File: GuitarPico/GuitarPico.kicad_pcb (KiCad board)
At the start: 2 copper layers, 100 x 100 mm, 125 parts, among them J1 INPUT, J2 INPUT, J3 OUTPUT, J4 OUTPUT, J5 Barrel_Jack_Switch, J6 VGA, J8 INPUT, J9 INPUT, Q1 2N3904, Q2 2N3904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

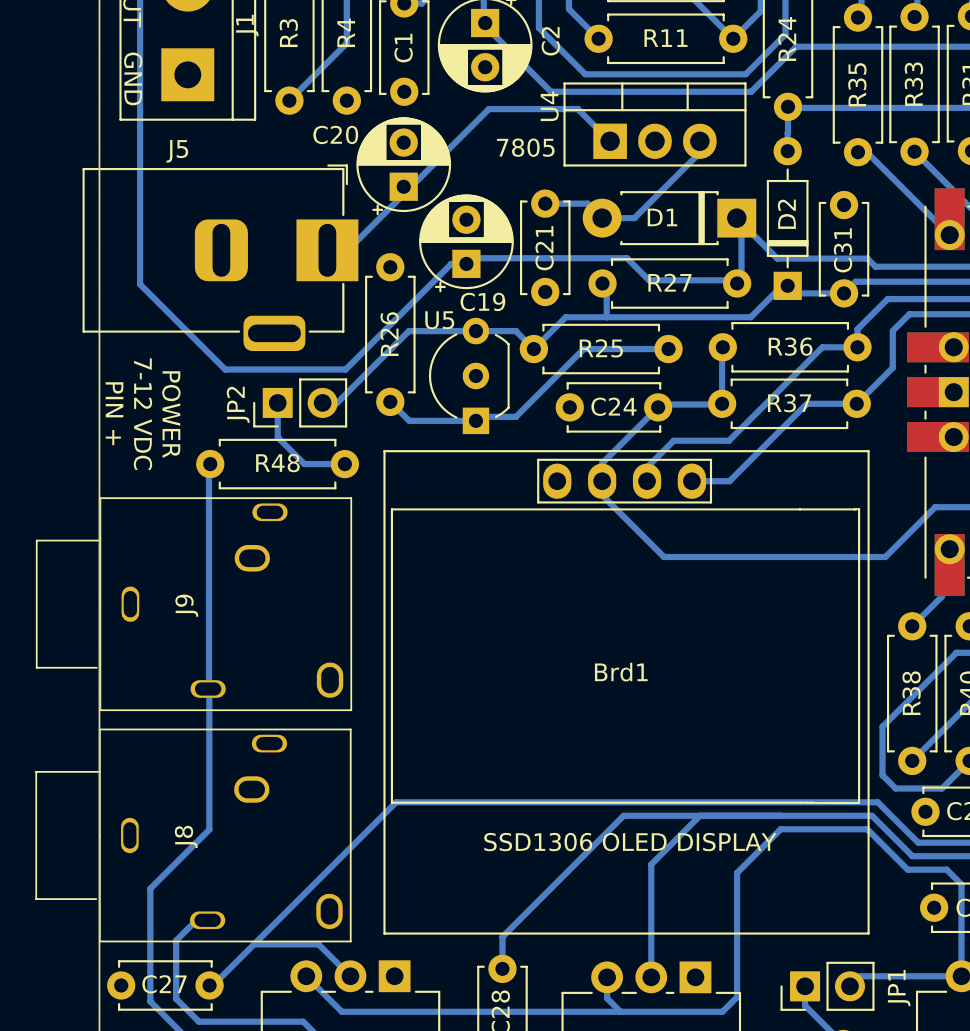
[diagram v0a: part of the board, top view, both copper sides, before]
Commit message: Added FIR Filter examples
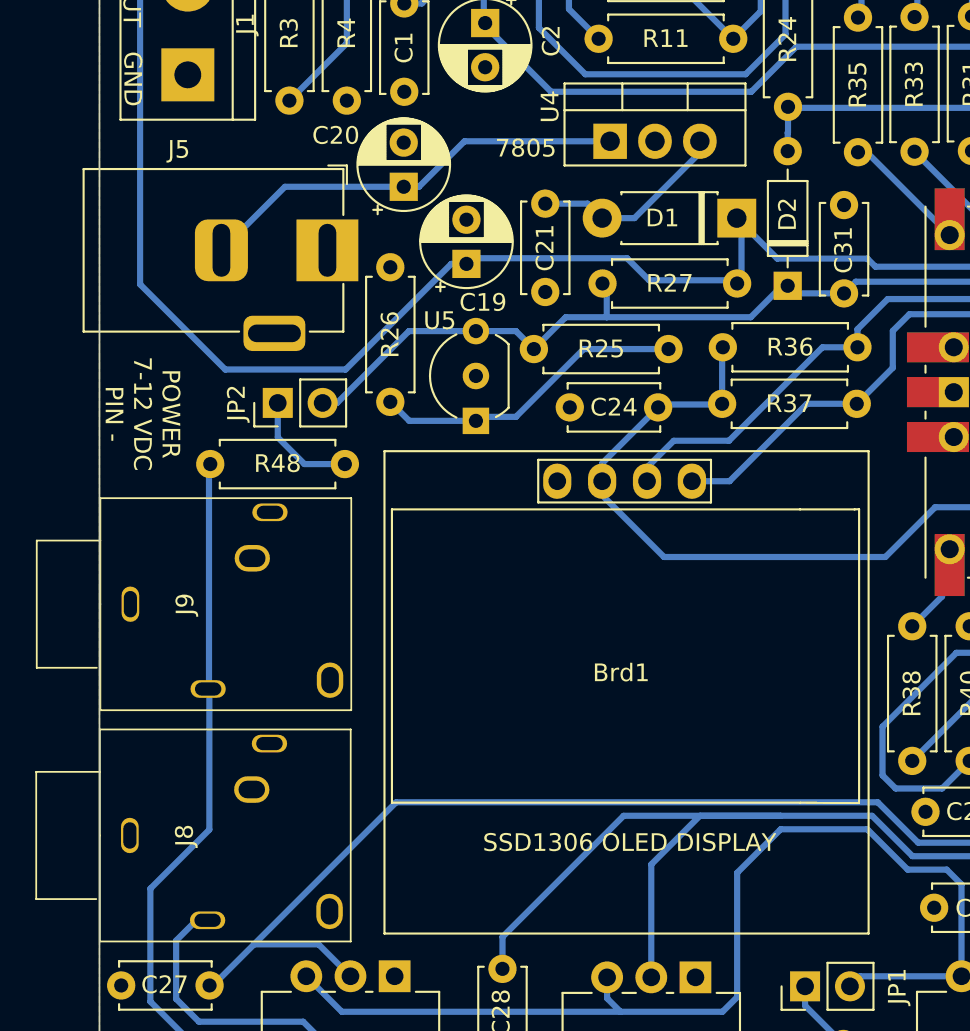
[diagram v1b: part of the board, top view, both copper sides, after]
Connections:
- J5 pad 1: Net-(C20-Pad1) -> GND
- J5 pad 2: GND -> Net-(C20-Pad1)
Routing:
- net Net-(C20-Pad1): track 20.1 -> 24.6 mm
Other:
- board text added: "POWER 7-12 VDC PIN -"
- board text removed: "POWER 7-12 VDC PIN +"
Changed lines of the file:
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@@
     (fp_line (start -0.003213 -4.505425) (end 0.8 -3.75) (layer "F.Fab") (width 0.1))
     (pad "1" thru_hole rect (at 0 0) (size 3.5 3.5) (drill oval 1 3) (layers *.Cu *.Mask)
-      (net 38 "Net-(C20-Pad1)") (pintype "passive"))
-    (pad "2" thru_hole roundrect (at -6 0) (size 3 3.5) (drill oval 1 3) (layers *.Cu *.Mask) (roundrect_rratio 0.25)
       (net 2 "GND") (pintype "passive"))
+    (pad "2" thru_hole roundrect (at -6 0) (size 3 3.5) (drill oval 1 3) (layers *.Cu *.Mask) (roundrect_rratio 0.25)
+      (net 38 "Net-(C20-Pad1)") (pintype "passive"))
     (pad "3" thru_hole roundrect (at -3 4.7) (size 3.5 2) (drill oval 3 1) (layers *.Cu *.Mask) (roundrect_rratio 0.25)
       (net 37 "unconnected-(J5-Pad3)") (pintype "passive"))
@@
       (effects (font (size 1 1) (thickness 0.15)))
     )
-    (fp_line (start 5.08 -11.811) (end 5.08 -9.398) (layer "F.SilkS") (width 0.12))
-    (fp_line (start -13.4 15) (end -13.4 -12.3) (layer "F.SilkS") (width 0.12))
+    (fp_line (start 10.122 7.595) (end 13.462 7.62) (layer "F.SilkS") (width 0.12))
+    (fp_line (start 13.462 7.62) (end 13.462 -9.017) (layer "F.SilkS") (width 0.12))
+    (fp_line (start 14 15) (end -13.4 15) (layer "F.SilkS") (width 0.12))
+    (fp_line (start 14 -12.3) (end 14 15) (layer "F.SilkS") (width 0.12))
+    (fp_line (start -12.978 -9.005) (end 10.122 -9.005) (layer "F.SilkS") (width 0.12))
     (fp_line (start 10.122 -9.005) (end 13.208 -9.005) (layer "F.SilkS") (width 0.12))
+    (fp_line (start -12.978 7.595) (end -12.978 -9.005) (layer "F.SilkS") (width 0.12))
+    (fp_line (start 10.122 7.595) (end -12.978 7.595) (layer "F.SilkS") (width 0.12))
     (fp_line (start 13.462 -9.017) (end 13.208 -9.005) (layer "F.SilkS") (width 0.12))
-    (fp_line (start 13.462 7.62) (end 13.462 -9.017) (layer "F.SilkS") (width 0.12))
+    (fp_line (start 5.08 -11.811) (end 5.08 -9.398) (layer "F.SilkS") (width 0.12))
     (fp_line (start 5.08 -9.398) (end -4.699 -9.398) (layer "F.SilkS") (width 0.12))
-    (fp_line (start 10.122 7.595) (end 13.462 7.62) (layer "F.SilkS") (width 0.12))
-    (fp_line (start 10.122 7.595) (end -12.978 7.595) (layer "F.SilkS") (width 0.12))
     (fp_line (start -4.699 -11.811) (end -4.699 -9.398) (layer "F.SilkS") (width 0.12))
-    (fp_line (start 14 -12.3) (end 14 15) (layer "F.SilkS") (width 0.12))
-    (fp_line (start -13.4 -12.3) (end 14 -12.3) (layer "F.SilkS") (width 0.12))
-    (fp_line (start 14 15) (end -13.4 15) (layer "F.SilkS") (width 0.12))
+    (fp_line (start -13.4 15) (end -13.4 -12.3) (layer "F.SilkS") (width 0.12))
     (fp_line (start -4.699 -11.811) (end 5.08 -11.811) (layer "F.SilkS") (width 0.12))
-    (fp_line (start -12.978 -9.005) (end 10.122 -9.005) (layer "F.SilkS") (width 0.12))
-    (fp_line (start -12.978 7.595) (end -12.978 -9.005) (layer "F.SilkS") (width 0.12))
-    (pad "" np_thru_hole oval (at -11 13) (size 3.6 3.1) (drill oval 3.5 3) (layers F&B.Cu *.Mask))
-    (pad "" np_thru_hole oval (at 12 -10.5) (size 3.6 3.1) (drill oval 3.5 3) (layers F&B.Cu *.Mask))
-    (pad "" np_thru_hole oval (at 12 13) (size 3.6 3.1) (drill oval 3.5 3) (layers F&B.Cu *.Mask))
-    (pad "" np_thru_hole oval (at -11 -10.5) (size 3.6 3.1) (drill oval 3.5 3) (layers F&B.Cu *.Mask))
+    (fp_line (start -13.4 -12.3) (end 14 -12.3) (layer "F.SilkS") (width 0.12))
+    (pad "" np_thru_hole oval (at -10.5 13) (size 5 3.1) (drill oval 4.8 3) (layers F&B.Cu *.Mask))
+    (pad "" np_thru_hole oval (at 11 -10.5) (size 5 3.1) (drill oval 4.8 3) (layers F&B.Cu *.Mask))
+    (pad "" np_thru_hole oval (at -10.5 -10.5) (size 5 3.1) (drill oval 4.8 3) (layers F&B.Cu *.Mask))
+    (pad "" np_thru_hole oval (at 11 13) (size 5 3.1) (drill oval 4.8 3) (layers F&B.Cu *.Mask))
     (pad "1" thru_hole oval (at -3.62 -10.6 90) (size 2 1.6) (drill 1) (layers *.Cu *.Mask)
       (net 2 "GND") (pinfunction "GND") (pintype "input"))
@@
     (effects (font (size 1 1) (thickness 0.15)))
   )
-  (gr_text "POWER\n7-12 VDC\nPIN +" (at 46.425 114.725 270) (layer "F.SilkS")
+  (gr_text "POWER\n7-12 VDC\nPIN -" (at 46.425 114.725 270) (layer "F.SilkS")
     (effects (font (size 1 1) (thickness 0.15)))
   )
@@
   (segment (start 69.23 102.83) (end 71.63 102.83) (width 0.35) (layer "B.Cu") (net 36))
   (segment (start 72.45 103.65) (end 74.28 103.65) (width 0.35) (layer "B.Cu") (net 36))
-  (segment (start 72.9 99.3) (end 71.08 97.48) (width 0.35) (layer "B.Cu") (net 38))
-  (segment (start 66.04 97.48) (end 58.048 105.472) (width 0.35) (layer "B.Cu") (net 38))
-  (segment (start 58.048 105.472) (end 56.902 105.472) (width 0.35) (layer "B.Cu") (net 38))
-  (segment (start 71.08 97.48) (end 66.04 97.48) (width 0.35) (layer "B.Cu") (net 38))
+  (segment (start 61.22 101.876) (end 62.084 101.876) (width 0.35) (layer "B.Cu") (net 38))
+  (segment (start 61.22 101.876) (end 54.498 101.876) (width 0.35) (layer "B.Cu") (net 38))
+  (segment (start 54.498 101.876) (end 50.902 105.472) (width 0.35) (layer "B.Cu") (net 38))
+  (segment (start 62.084 101.876) (end 64.66 99.3) (width 0.35) (layer "B.Cu") (net 38))
+  (segment (start 64.66 99.3) (end 72.9 99.3) (width 0.35) (layer "B.Cu") (net 38))
   (segment (start 70.57 88.34) (end 70.57 91.82) (width 0.35) (layer "B.Cu") (net 39))
   (segment (start 73 81.75) (end 73.75 82.5) (width 0.35) (layer "B.Cu") (net 39))

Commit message: First example of guitarpico project
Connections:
- R12 pad 2: Net-(R12-Pad2) -> Net-(C9-Pad1)
- R24 pad 2: Net-(R12-Pad2) -> Net-(C9-Pad1)
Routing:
- net Net-(C9-Pad1): track 17.8 -> 43.4 mm
- net Net-(R12-Pad2): track 23.8 -> 0.00 mm

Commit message: Working pass thru
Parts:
- added C32: 220 uF, Capacitor_THT:CP_Radial_D5.0mm_P2.50mm, F.Cu at (79.6, 123.2)
- added C33: 220 uF, Capacitor_THT:CP_Radial_D5.0mm_P2.50mm, F.Cu at (79.5, 131.0)
- added R58: 10R, Resistor_THT:R_Axial_DIN0207_L6.3mm_D2.5mm_P7.62mm_Horizontal, F.Cu at (85.0, 123.5)
- C9: value 47 pF -> 220 pF
- R24: value 10k -> 100
- R9: value 10k -> 47k
- moved R36 1.18 mm to (80.0, 111.9)
- moved R37 1.16 mm to (87.6, 115.0)
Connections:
- Brd1 pad 2: +3V3 -> Net-(Brd1-Pad2)
- C24 pad 2: +3V3 -> Net-(Brd1-Pad2)
- RV1 pad 1: Net-(C7-Pad2) -> Net-(R5-Pad1)
- RV1 pad 3: Net-(R5-Pad1) -> Net-(C7-Pad2)
- RV2 pad 1: Net-(C17-Pad1) -> Net-(R17-Pad1)
- RV2 pad 3: Net-(R17-Pad1) -> Net-(C17-Pad1)
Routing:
- net Net-(Brd1-Pad2): track 0.00 -> 35.5 mm
- net Net-(R17-Pad1): track 47.6 -> 61.3 mm
- net +3V3: track 135.5 -> 122.7 mm
- net Net-(C17-Pad1): track 61.2 -> 51.2 mm
- net SDA: track 38.1 -> 46.8 mm
- net SCL: track 38.2 -> 42.6 mm
- net Net-(C7-Pad2): track 35.8 -> 39.1 mm
- net Net-(R5-Pad1): track 36.6 -> 34.7 mm
- net VREF: track 231.1 -> 230.4 mm

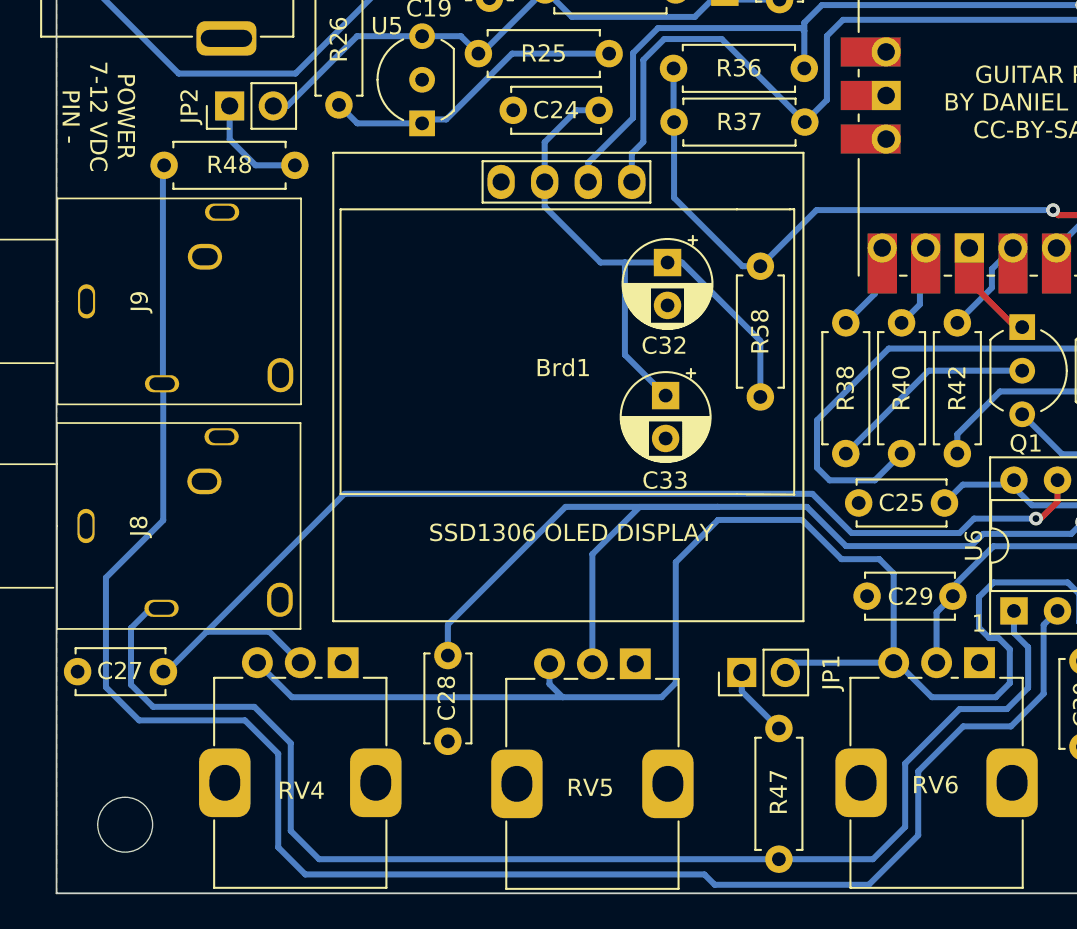
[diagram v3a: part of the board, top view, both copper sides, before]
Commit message: Added ui elements
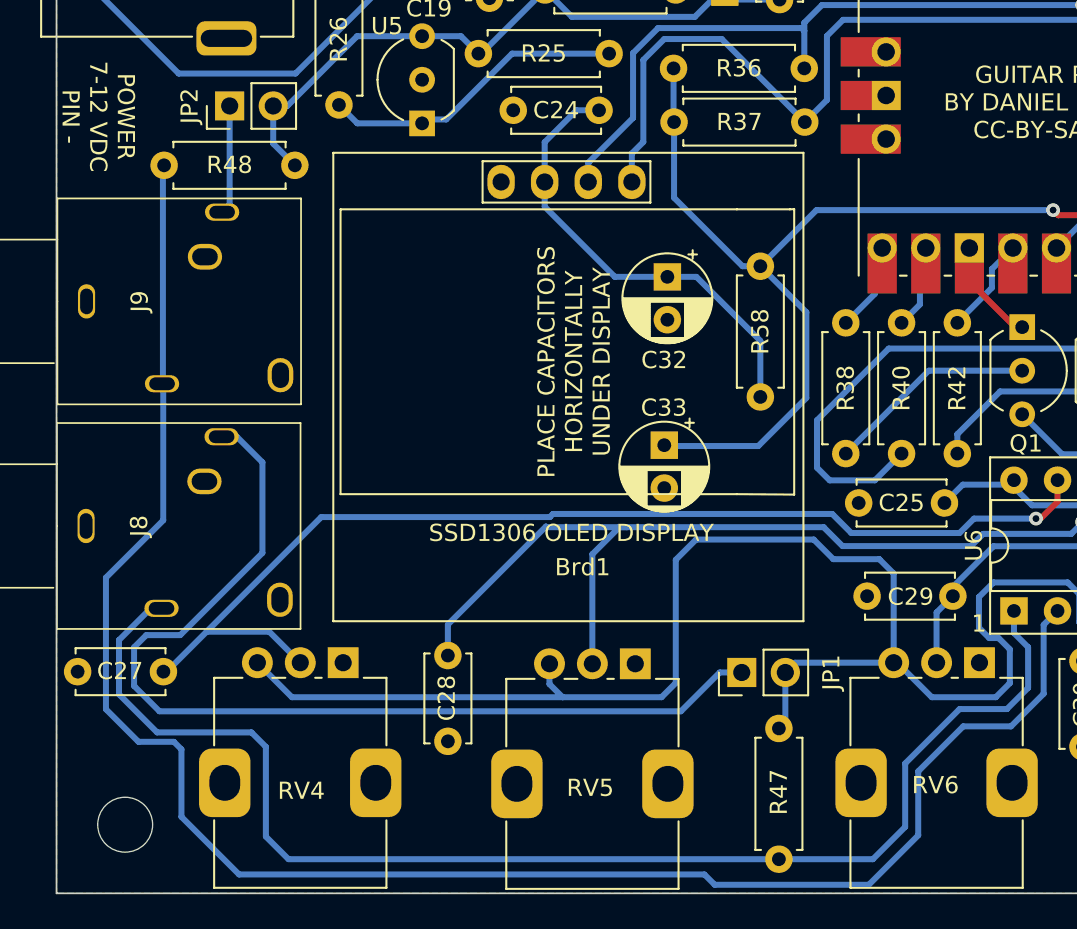
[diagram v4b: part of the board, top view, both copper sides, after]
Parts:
- R47, R48: value 10k -> NC
- moved C33 2.89 mm to (79.4, 133.9)
- moved C32 0.84 mm to (79.6, 124.1)
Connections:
- C33 pad 1: Net-(Brd1-Pad2) -> +3V3
- J8 pad S1: unconnected-(J8-PadS1) -> Net-(J8-PadS1)
- J9 pad S1: unconnected-(J9-PadS1) -> Net-(JP2-Pad1)
- JP1 pad 1: Net-(JP1-Pad1) -> Net-(J8-PadS1)
- R47 pad 1: Net-(JP1-Pad1) -> VREF
- R48 pad 1: Net-(JP2-Pad1) -> VREF
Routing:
- net Net-(J8-PadS1): track 0.00 -> 57.3 mm
- net +3V3: track 122.7 -> 141.0 mm
- net Net-(Brd1-Pad2): track 35.5 -> 26.8 mm
- net Net-(C28-Pad2): track 60.9 -> 54.2 mm
- net VREF: track 230.4 -> 236.9 mm
- net Net-(JP1-Pad1): track 4.16 -> 0.00 mm
- net Net-(J8-PadT1): track 76.2 -> 77.6 mm
- net Net-(C27-Pad2): track 65.6 -> 64.6 mm
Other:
- board text added: "PLACE CAPACITORS HORIZONTALLY UNDER DISPLAY"

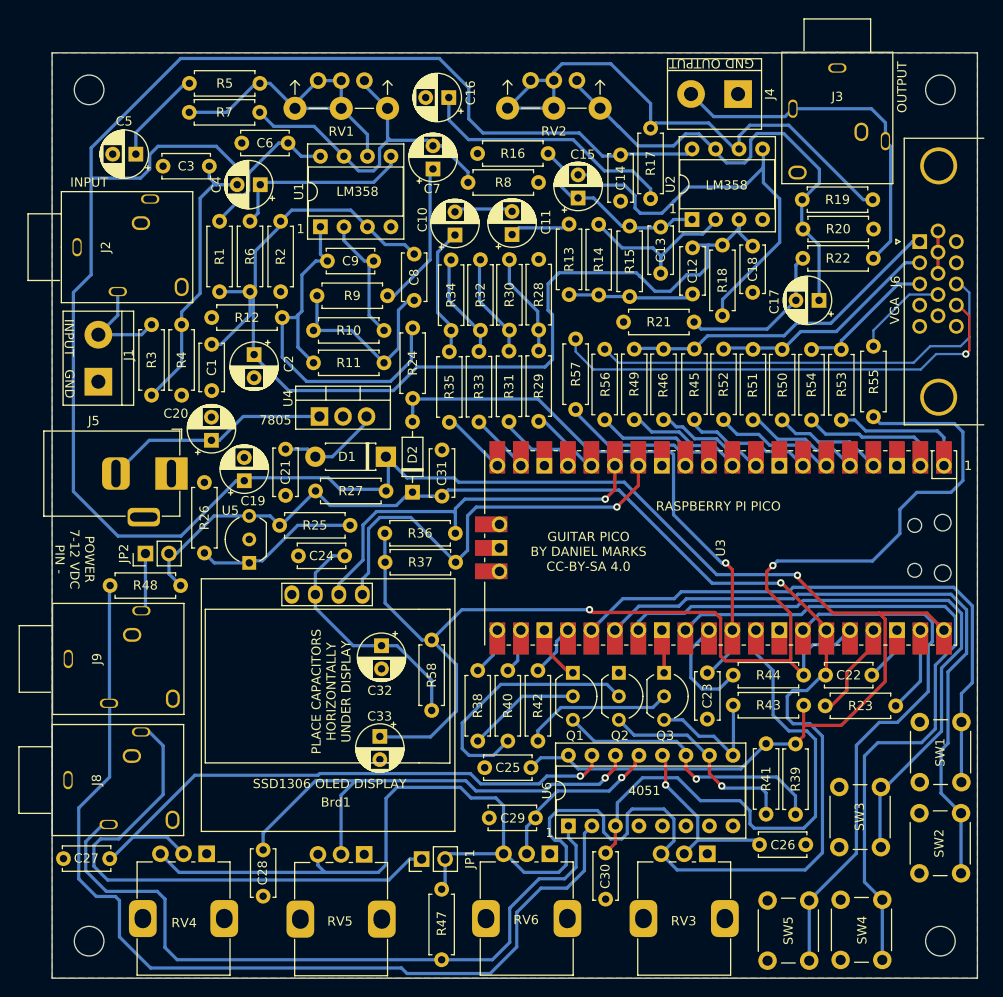
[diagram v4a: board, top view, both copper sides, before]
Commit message: can now edit parameters
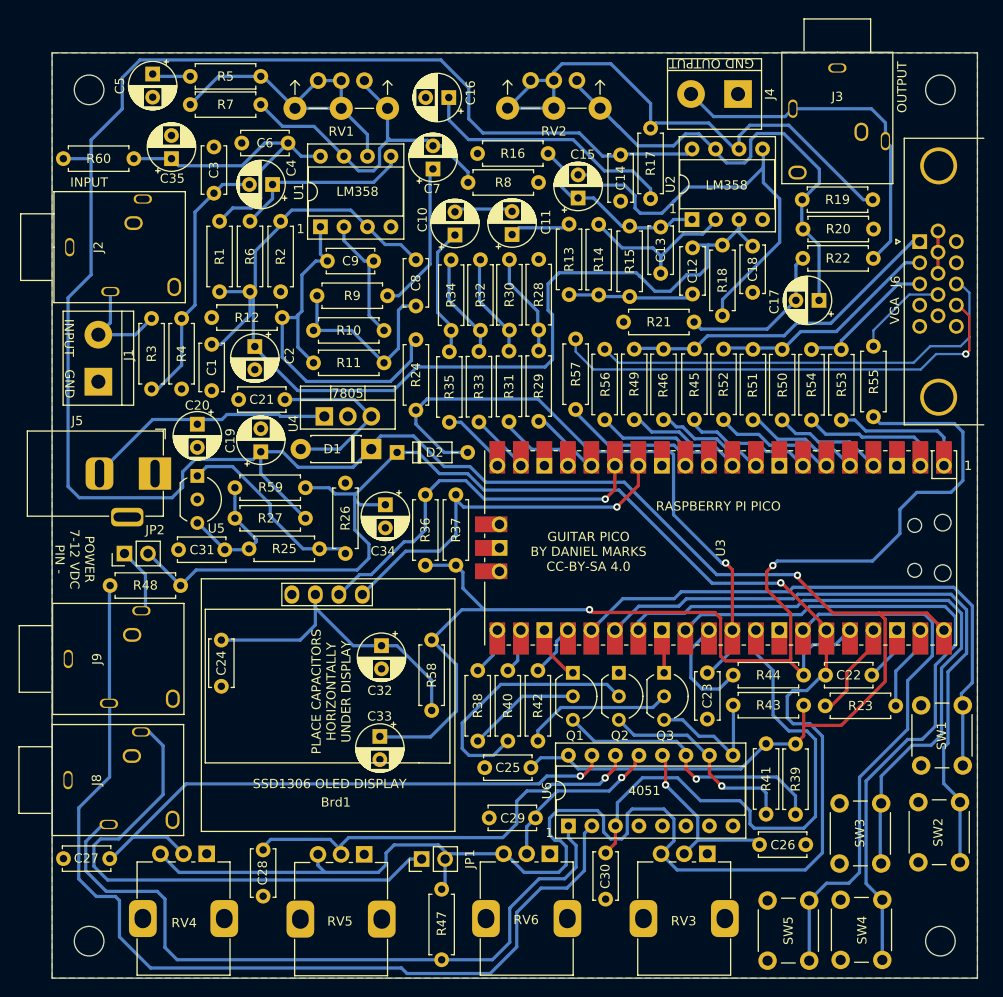
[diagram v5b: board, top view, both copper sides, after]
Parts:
- added C34: 100 uF, Capacitor_THT:CP_Radial_D5.0mm_P2.50mm, F.Cu at (80.0, 108.8)
- added C35: 100 uF, Capacitor_THT:CP_Radial_D5.0mm_P2.50mm, F.Cu at (56.9, 71.4)
- added R59: 10R, Resistor_THT:R_Axial_DIN0207_L6.3mm_D2.5mm_P7.62mm_Horizontal, F.Cu at (63.8, 107.0)
- added R60: 10R, Resistor_THT:R_Axial_DIN0207_L6.3mm_D2.5mm_P7.62mm_Horizontal, F.Cu at (45.2, 71.4)
- C3: value 100 pF -> 1000 pF
- R17, RV1, RV2: value 100k -> 10k
- R24: value 100 -> 100R
- R5: value 2k2 -> 220R
- moved C31 30.5 mm to (57.7, 113.7), turned to 0 degrees
- moved C24 16.4 mm to (62.3, 128.5), turned to 90 degrees
- moved R26 15.2 mm to (75.7, 106.5)
- moved U5 10.9 mm to (59.7, 105.7), turned to -90 degrees
- moved R27 9.20 mm to (63.8, 110.3)
- moved C5 8.85 mm to (54.9, 62.3), turned to -90 degrees
- moved R37 7.29 mm to (87.6, 107.8), turned to -90 degrees
- moved R36 5.58 mm to (84.3, 115.4), turned to 90 degrees
- moved C21 5.36 mm to (69.2, 97.5), turned to 180 degrees
- moved D2 4.61 mm to (81.3, 103.2), turned to 0 degrees
- moved R25 4.17 mm to (72.9, 113.6)
- moved C19 3.60 mm to (66.6, 103.1)
- moved C3 2.96 mm to (61.5, 75.2), turned to 90 degrees
- moved C20 2.31 mm to (59.7, 100.1), turned to -90 degrees
- moved JP2 2.27 mm to (51.8, 114.1)
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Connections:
- C31 pad 2: VREF -> Net-(C31-Pad2)
- C6 pad 1: +5V -> Net-(R1-Pad2)
- J2 pad G: GND -> unconnected-(J2-PadG)
- R1 pad 2: +5V -> Net-(R1-Pad2)
- R25 pad 2: VREF -> Net-(C31-Pad2)
- R27 pad 1: VREF -> Net-(C31-Pad2)
- U1 pad 8: +5V -> Net-(R1-Pad2)
- U5 pad 3: VREF -> Net-(C31-Pad2)
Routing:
- net Net-(R1-Pad2): track 0.00 -> 34.8 mm
- net +5V: track 315.5 -> 291.3 mm
- net Net-(C31-Pad2): track 0.00 -> 14.7 mm
- net Net-(C21-Pad1): track 11.3 -> 19.3 mm
- net Net-(Brd1-Pad2): track 26.8 -> 34.6 mm
- net Net-(C28-Pad2): track 54.2 -> 46.9 mm
- net Net-(C5-Pad1): track 10.3 -> 4.17 mm
- net SDA: track 46.8 -> 40.8 mm
- net TOADC: track 61.0 -> 66.9 mm
- net +3V3: track 141.0 -> 136.0 mm
- net Net-(R25-Pad1): track 17.5 -> 21.1 mm
- net Net-(C20-Pad1): track 24.6 -> 27.5 mm
- net BUTTON3: track 67.7 -> 70.4 mm
- net BUTTON4: track 75.4 -> 73.4 mm
- net Net-(C3-Pad1): track 30.4 -> 28.6 mm
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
